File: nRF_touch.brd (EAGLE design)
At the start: 46 x 77.5 mm, 35 parts, among them J1 CORTEX_DEBUG_PTH, T1 BSS84, T2 BC847, U1 ADP160, U2 AT42QT1010-TSHR

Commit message: First routing
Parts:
- added C9: 0.1uF, SparkFun-Capacitors:0603
- added LED1: (no value), adafruit:CHIPLED_1206
- added R12: 330, SparkFun-Resistors:0603
- moved J1 36.3 mm to (44.2, 31.0), turned to 90 degrees
- moved J2 13.5 mm to (44.3, 13.2), turned to 90 degrees
- moved R3 1.31 mm to (40.6, 51.9), turned to 180 degrees
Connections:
- new net N$1: R12.2, U$1.D6
- new net N$2: LED1.A, R12.1
- net GND: now also C9.2, LED1.C
- net LDO_EN: now also C9.1
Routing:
- net VCC: track 0.00 -> 157.2 mm, vias 0 -> 8
- net 5V: track 0.00 -> 75.1 mm, vias 0 -> 4
- net GND: track 0.00 -> 61.6 mm, vias 0 -> 1
- net SPIM_DO: track 0.00 -> 49.7 mm, vias 0 -> 2
- net SPIM_SCK: track 0.00 -> 45.2 mm, vias 0 -> 2
- net AT42_OUT: track 0.00 -> 41.6 mm, vias 0 -> 2
- net SCL: track 0.00 -> 37.5 mm, vias 0 -> 1
- net SDA: track 0.00 -> 36.2 mm, vias 0 -> 1
- net SST_CS: track 0.00 -> 36.0 mm, vias 0 -> 2
- net SPIS_SCK: track 0.00 -> 31.5 mm, vias 0 -> 2
- net SPIM_DIN: track 0.00 -> 29.5 mm, vias 0 -> 2
- net SHARP_CS: track 0.00 -> 27.8 mm, vias 0 -> 2
- net 5150_CS: track 0.00 -> 27.0 mm, vias 0 -> 2
- net NRF_EN: track 0.00 -> 21.2 mm, vias 0 -> 2
- net SPIS_MI: track 0.00 -> 20.3 mm, vias 0 -> 2
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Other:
- board size 46 x 77.5 mm -> 46.3 x 77.5 mm

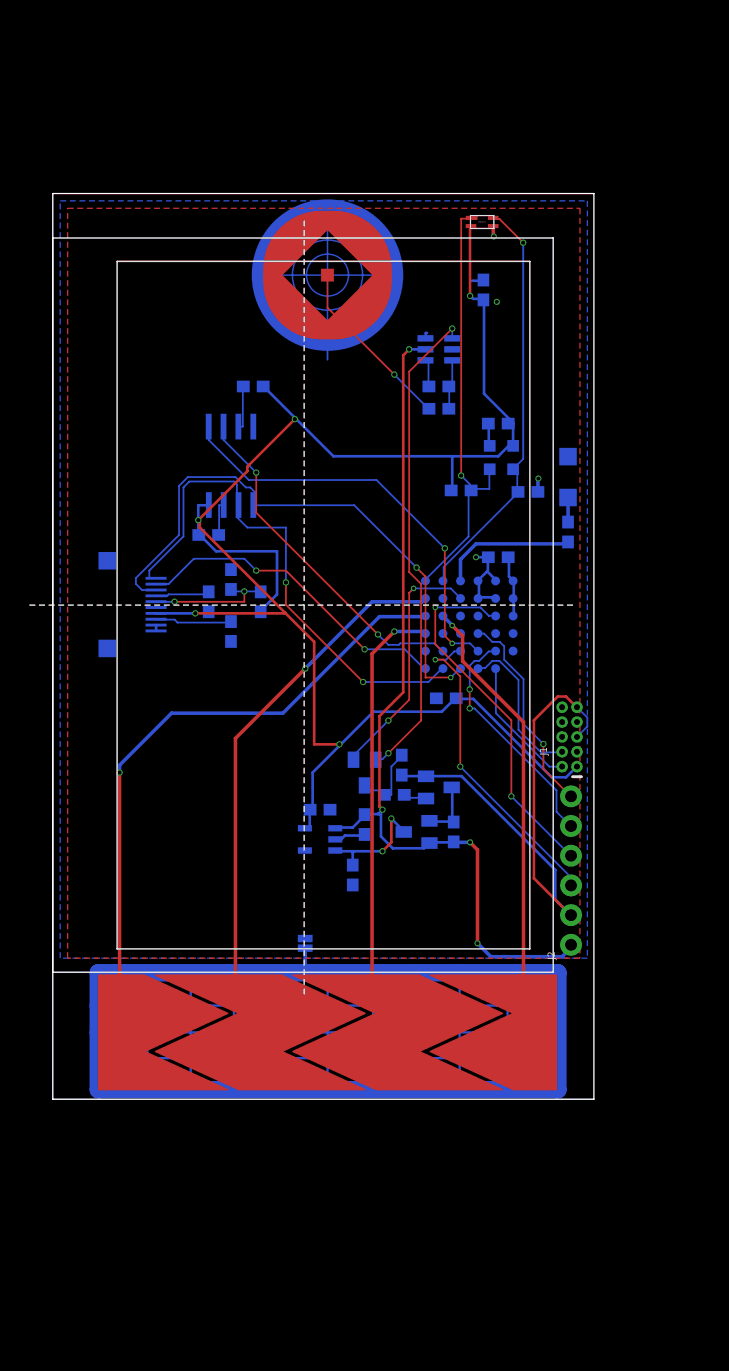
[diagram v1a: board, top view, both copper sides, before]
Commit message: Modified stop on qtouch
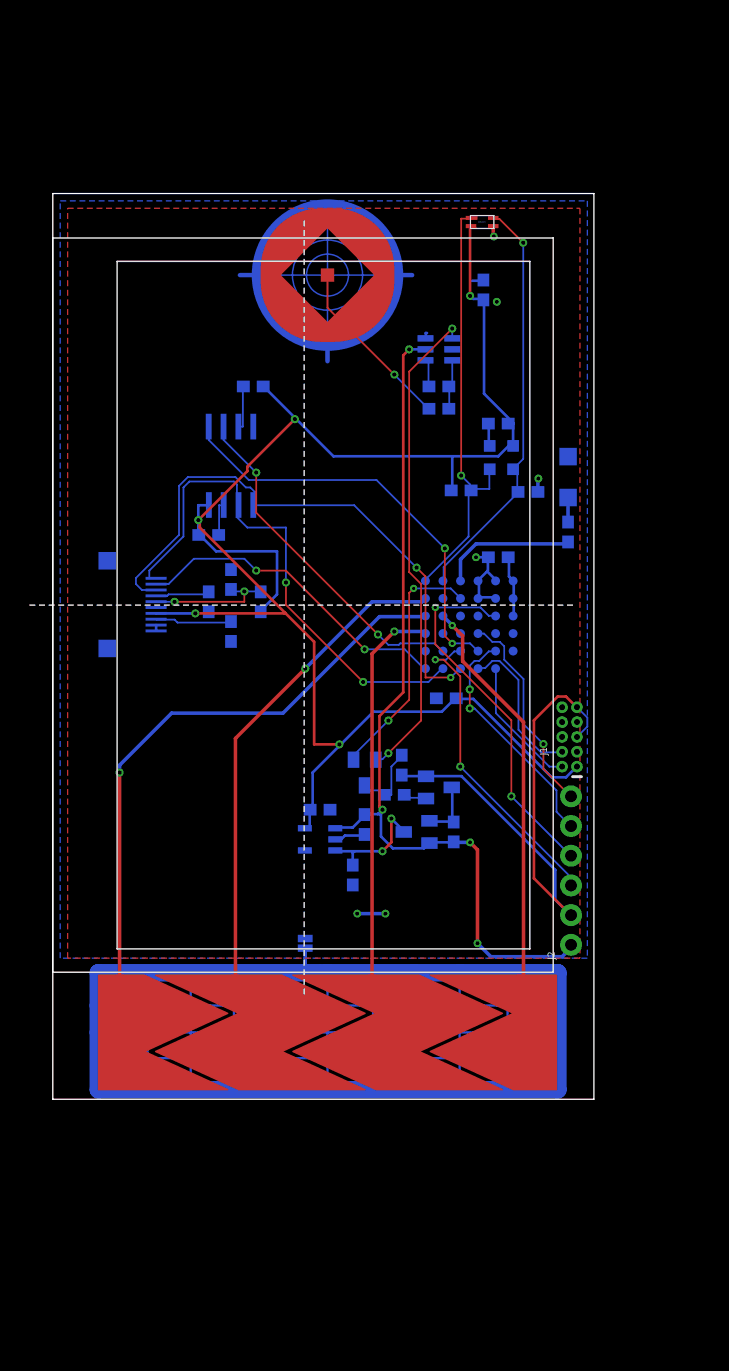
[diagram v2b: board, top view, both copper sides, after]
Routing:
- net GND: track 61.6 -> 65.5 mm
- net VCC: track 157.2 -> 159.6 mm, vias 8 -> 10
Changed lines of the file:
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@@
 <layers>
 <layer number="1" name="Top" color="4" fill="1" visible="yes" active="yes"/>
-<layer number="2" name="Route2" color="1" fill="3" visible="no" active="yes"/>
+<layer number="2" name="Route2" color="1" fill="3" visible="no" active="no"/>
 <layer number="3" name="Route3" color="4" fill="3" visible="no" active="no"/>
 <layer number="4" name="Route4" color="1" fill="4" visible="no" active="no"/>
@@
 <layer number="13" name="Route13" color="4" fill="5" visible="no" active="no"/>
 <layer number="14" name="Route14" color="1" fill="6" visible="no" active="no"/>
-<layer number="15" name="Route15" color="4" fill="6" visible="no" active="yes"/>
+<layer number="15" name="Route15" color="4" fill="6" visible="no" active="no"/>
 <layer number="16" name="Bottom" color="1" fill="1" visible="yes" active="yes"/>
 <layer number="17" name="Pads" color="2" fill="1" visible="yes" active="yes"/>
@@
 <layer number="41" name="tRestrict" color="4" fill="10" visible="yes" active="yes"/>
 <layer number="42" name="bRestrict" color="1" fill="10" visible="yes" active="yes"/>
-<layer number="43" name="vRestrict" color="2" fill="10" visible="yes" active="yes"/>
+<layer number="43" name="vRestrict" color="2" fill="10" visible="no" active="yes"/>
 <layer number="44" name="Drills" color="7" fill="1" visible="no" active="yes"/>
 <layer number="45" name="Holes" color="7" fill="1" visible="no" active="yes"/>
@@
 </class>
 </classes>
-<designrules name="OSHPark-4layer">
+<designrules name="oshpark-2layer">
 <description language="de">&lt;b&gt;EAGLE Design Rules&lt;/b&gt;
 &lt;p&gt;
@@
 &lt;p&gt;
 Please make sure your boards conform to these design rules.</description>
-<param name="layerSetup" value="(1*2*15*16)"/>
-<param name="mtCopper" value="0.035559375mm 0.01778125mm 0.0356mm 0.0356mm 0.0356mm 0.0356mm 0.0356mm 0.0356mm 0.0356mm 0.0356mm 0.0356mm 0.0356mm 0.0356mm 0.0356mm 0.01778125mm 0.035559375mm"/>
-<param name="mtIsolate" value="0.17018125mm 47mil 0.2007mm 0.1499mm 0.2007mm 0.1499mm 0.2007mm 0.1499mm 0.2007mm 0.1499mm 0.2007mm 0.1499mm 0.2007mm 0.1499mm 0.17018125mm"/>
-<param name="mdWireWire" value="5mil"/>
-<param name="mdWirePad" value="5mil"/>
-<param name="mdWireVia" value="5mil"/>
-<param name="mdPadPad" value="5mil"/>
-<param name="mdPadVia" value="5mil"/>
-<param name="mdViaVia" value="5mil"/>
-<param name="mdSmdPad" value="5mil"/>
-<param name="mdSmdVia" value="5mil"/>
-<param name="mdSmdSmd" value="5mil"/>
+<param name="layerSetup" value="(1*16)"/>
+<param name="mtCopper" value="0.0356mm 0.0356mm 0.0356mm 0.0356mm 0.0356mm 0.0356mm 0.0356mm 0.0356mm 0.0356mm 0.0356mm 0.0356mm 0.0356mm 0.0356mm 0.0356mm 0.0356mm 0.0356mm"/>
+<param name="mtIsolate" value="1.5011mm 0.1499mm 0.2007mm 0.1499mm 0.2007mm 0.1499mm 0.2007mm 0.1499mm 0.2007mm 0.1499mm 0.2007mm 0.1499mm 0.2007mm 0.1499mm 0.2007mm"/>
+<param name="mdWireWire" value="6mil"/>
+<param name="mdWirePad" value="6mil"/>
+<param name="mdWireVia" value="6mil"/>
+<param name="mdPadPad" value="6mil"/>
+<param name="mdPadVia" value="6mil"/>
+<param name="mdViaVia" value="6mil"/>
+<param name="mdSmdPad" value="6mil"/>
+<param name="mdSmdVia" value="6mil"/>
+<param name="mdSmdSmd" value="6mil"/>
 <param name="mdViaViaSameLayer" value="8mil"/>
 <param name="mnLayersViaInSmd" value="2"/>
@@
 <param name="mdDrill" value="6mil"/>
 <param name="mdSmdStop" value="0mil"/>
-<param name="msWidth" value="5mil"/>
-<param name="msDrill" value="10mil"/>
-<param name="msMicroVia" value="10mil"/>
+<param name="msWidth" value="6mil"/>
+<param name="msDrill" value="13mil"/>
+<param name="msMicroVia" value="13mil"/>
 <param name="msBlindViaRatio" value="0.5"/>
 <param name="rvPadTop" value="0.25"/>
@@
 <param name="rvMicroViaOuter" value="0.25"/>
 <param name="rvMicroViaInner" value="0.25"/>
-<param name="rlMinPadTop" value="4mil"/>
+<param name="rlMinPadTop" value="7mil"/>
 <param name="rlMaxPadTop" value="20mil"/>
-<param name="rlMinPadInner" value="4mil"/>
+<param name="rlMinPadInner" value="7mil"/>
 <param name="rlMaxPadInner" value="20mil"/>
-<param name="rlMinPadBottom" value="4mil"/>
+<param name="rlMinPadBottom" value="7mil"/>
 <param name="rlMaxPadBottom" value="20mil"/>
-<param name="rlMinViaOuter" value="4mil"/>
+<param name="rlMinViaOuter" value="7mil"/>
 <param name="rlMaxViaOuter" value="20mil"/>
-<param name="rlMinViaInner" value="4mil"/>
+<param name="rlMinViaInner" value="7mil"/>
 <param name="rlMaxViaInner" value="20mil"/>
 <param name="rlMinMicroViaOuter" value="4mil"/>
@@
 <via x="36.195" y="46.355" extent="1-16" drill="0.3302"/>
 <wire x1="36.195" y1="46.355" x2="37.25" y2="46.355" width="0.2286" layer="16"/>
+<via x="26.035" y="15.875" extent="1-16" drill="0.3302"/>
+<via x="28.448" y="15.875" extent="1-16" drill="0.3302"/>
+<wire x1="26.035" y1="15.875" x2="28.448" y2="15.875" width="0.3048" layer="16"/>
 </signal>
 <signal name="GND" class="1">
@@
 <wire x1="37.669" y1="73.837" x2="37.719" y2="73.787" width="0.3048" layer="1"/>
 <wire x1="23.495" y1="64.516" x2="23.495" y2="64.397" width="0.1524" layer="16"/>
-<wire x1="23.495" y1="64.397" x2="23.495" y2="63.246" width="0.1524" layer="16"/>
+<wire x1="23.495" y1="64.397" x2="23.495" y2="64.389" width="0.1524" layer="16"/>
+<wire x1="23.495" y1="64.389" x2="23.495" y2="63.246" width="0.1524" layer="16"/>
 <wire x1="44.831" y1="33.528" x2="45.72" y2="32.639" width="0.1524" layer="16"/>
 <wire x1="45.72" y1="32.639" x2="45.72" y2="31.877" width="0.1524" layer="16"/>
 <wire x1="45.72" y1="31.877" x2="44.831" y2="30.988" width="0.1524" layer="16"/>
+<wire x1="23.495" y1="63.119" x2="23.495" y2="64.389" width="0.381" layer="16"/>
+<wire x1="16.002" y1="70.485" x2="17.399" y2="70.485" width="0.381" layer="16"/>
+<wire x1="29.464" y1="70.485" x2="30.734" y2="70.485" width="0.381" layer="16"/>
 </signal>
 <signal name="AIN2">

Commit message: Improvements #1
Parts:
- added C10: 0.1uF, SparkFun-Capacitors:0603
- U$4: value SHARP27_REV -> SHARP27
- moved R5 9.19 mm to (10.1, 47.6), turned to 45 degrees
- moved LED1 4.32 mm to (44.1, 57.5)
- moved R12 3.56 mm to (44.1, 52.1)
- moved U$4 0.44 mm to (6.16, 42.2)
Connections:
- net 5V: now also C10.2
- net DISP: now also U$4.5; no longer U$4.6
- net EXTCOMM: now also U$4.4; no longer U$4.7
- net EXTMODE: now also U$4.8; no longer U$4.3
- net GND: now also C10.1, U$4.10, U$4.9; no longer U$4.1, U$4.2
- net SHARP_CS: now also U$4.3; no longer U$4.9
- net SPIM_DO: now also U$4.2; no longer U$4.8
- net SPIM_SCK: now also U$4.1; no longer U$4.10
- net VCC: now also U$4.6, U$4.7; no longer U$4.4
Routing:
- net VCC: track 159.6 -> 50.1 mm, vias 10 -> 13
- net SPIM_SCK: track 45.2 -> 39.4 mm, vias 2 -> 3
- net GND: track 65.5 -> 69.8 mm, vias 1 -> 3
- net 5V: track 75.1 -> 78.6 mm
- net SPIM_DO: track 49.7 -> 52.3 mm
- net EXTMODE: track 6.61 -> 5.08 mm
- net N$1: track 11.7 -> 13.1 mm
- net N$2: track 2.10 -> 2.86 mm
- net DISP: track 11.1 -> 10.4 mm, vias 2 -> 0

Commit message: Optimizations
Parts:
- moved JP1 1.98 mm to (22.9, 11.8)
- moved C5 0.38 mm to (33.3, 34.3)
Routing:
- net N$10: track 2.76 -> 0.03 mm
- net LDO_EN: track 10.1 -> 8.40 mm
- net SPIM_SCK: track 39.4 -> 41.0 mm
- net SCL: track 37.5 -> 36.5 mm
- net VCC: track 50.1 -> 50.6 mm

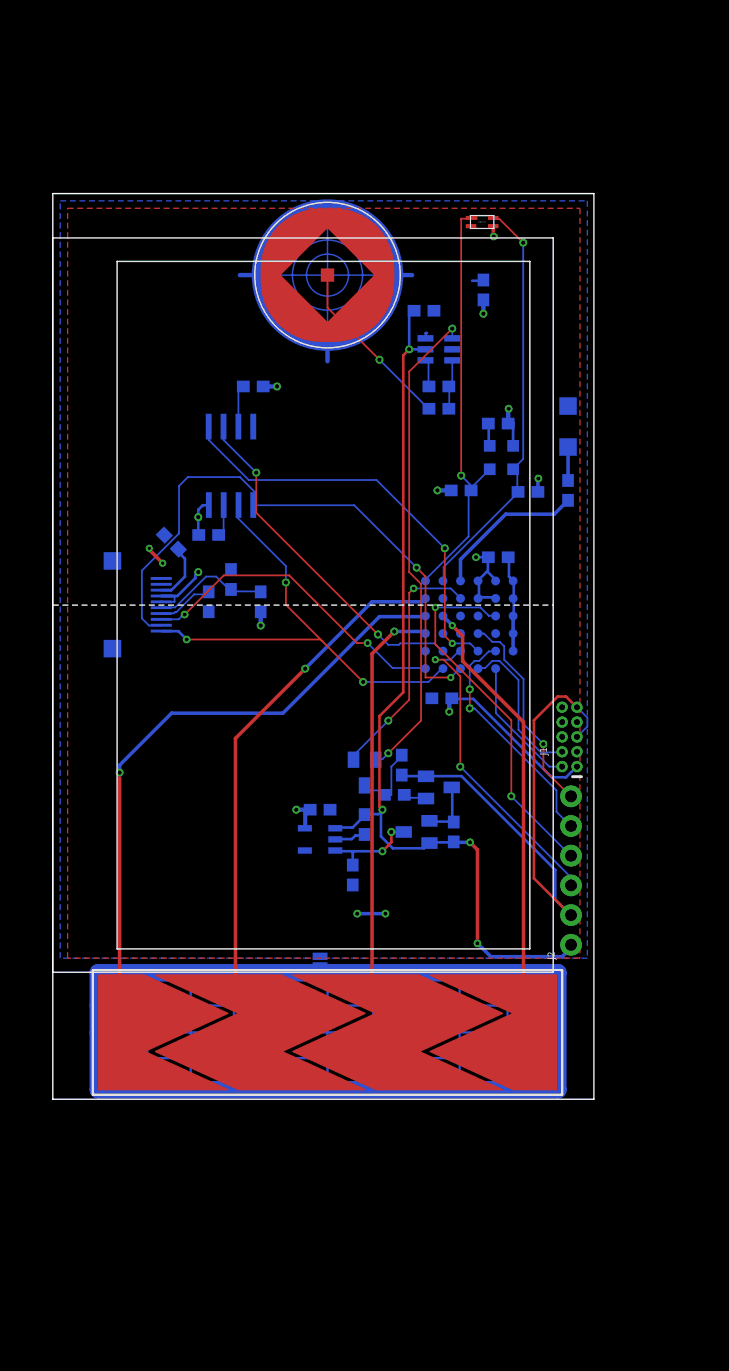
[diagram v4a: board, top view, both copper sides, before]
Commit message: Addition of neopixel and change in logic
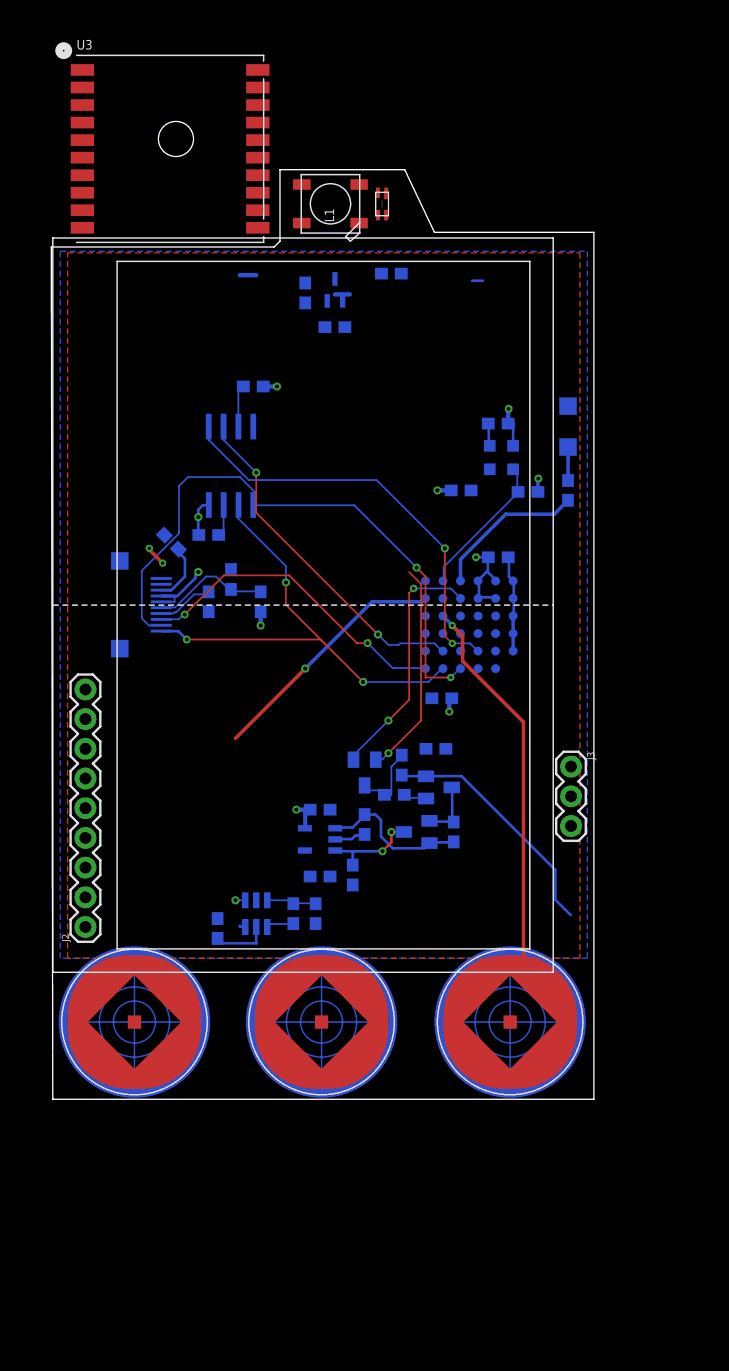
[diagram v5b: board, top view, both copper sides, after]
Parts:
- removed J1: CORTEX_DEBUG_PTH, SparkFun-Connectors:2X5-PTH-1.27MM
- removed JP1: (no value), SparkFun-Retired:SJ_2S
- added C11: 1uF, SparkFun-Capacitors:0603
- added J3: (no value), SparkFun-Connectors:1X03
- added L1: WS2812B, adafruit:WS2812B
- added Q1: BSS138BKW, BSS138:SOT65P210X110-3N
- added R13: 47k, SparkFun-Resistors:0603
- added R14, R15: 10k, SparkFun-Resistors:0603
- added S3: L_BUTTON, qtouch:BUTTON
- added U3: (no value), adafruit:FGPMMOPA6H
- D1: value BAT754C -> BAT54C
- J2: device SparkFun-Connectors:1X06_NO_SILK -> SparkFun-Connectors:1X09
- S1: value SLIDER -> L_BUTTON; device qtouch:SLIDER -> qtouch:BUTTON
- T2: value BC847 -> BC847/2N7002
- moved S2 63.9 mm to (23.0, 6.60)
- moved C10 55.7 mm to (14.1, 14.6), turned to 270 degrees
- moved U2 50.7 mm to (17.4, 15.9), turned to 270 degrees
- moved C7 46.8 mm to (20.6, 15.9), turned to 90 degrees
- moved R11 44.4 mm to (22.5, 15.9), turned to 90 degrees
- moved J2 41.6 mm to (2.79, 14.7)
- moved S1 15.6 mm to (39.1, 6.60)
- moved U$2 9.95 mm to (27.8, 75.6), turned to 90 degrees
- moved C3 8.00 mm to (29.0, 70.6), turned to 0 degrees
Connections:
- removed net AIN2: S1.P$1, U$1.F4
- removed net AIN4: S1.P$3, U$1.F3
- removed net LDO_EN: C9.1, T1.3, U1.3
- removed net N$10: JP1.1, S1.GND
- new net NEO_DIN: L1.4-DIN, Q1.3, R14.1
- new net NEO_PIN: Q1.2, R15.1, U$1.F1
- new net SW_POWER: C9.1, L1.1-VDD, R13.2, R14.2, T1.3, U1.3
- net AIN3: now also S3.P$1; no longer S1.P$2
- net AIN5: now also S1.P$1; no longer S1.P$4
- net GND: now also C11.2, L1.3-GND, R13.1, S1.GND, S3.GND; no longer J1.3, J1.5, J1.9, JP1.2
- net N$11: now also C11.1
- net SHARP_CS: no longer U$1.F1
- net SPIS_MI: no longer U$1.B2
- net SPIS_MO: no longer U$1.C3
- net SPIS_SCK: no longer U$1.B4
- net SST_CS: now also J2.7; no longer U$1.C2
- net SWDCLK: now also J3.2; no longer J1.4
- net SWDIO: now also J3.1; no longer J1.2
- net VCC: now also J2.9, J3.3, Q1.1, R15.2; no longer J1.1
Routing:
- net 5V: track 78.5 -> 17.9 mm, vias 4 -> 0
- net AIN2: track 50.0 -> 0.00 mm, vias 1 -> 0
- net SCL: track 36.5 -> 0.00 mm, vias 1 -> 0
- net AIN4: track 33.5 -> 0.00 mm, vias 1 -> 0
- net SPIS_SCK: track 31.5 -> 0.00 mm, vias 2 -> 0
- net GND: track 69.8 -> 40.0 mm, vias 3 -> 2
- net 5150_CS: track 27.0 -> 0.00 mm, vias 2 -> 0
- net SDA: track 36.2 -> 13.0 mm, vias 1 -> 0
- net AT42_OUT: track 41.6 -> 19.2 mm
- net AIN3: track 42.0 -> 21.2 mm
- net SPIS_MI: track 20.3 -> 0.00 mm, vias 2 -> 0
- net SPIS_MO: track 17.9 -> 0.00 mm, vias 1 -> 0
- net VCC: track 50.6 -> 32.8 mm, vias 13 -> 10
- net PAD: track 15.0 -> 0.04 mm, vias 1 -> 0
- net SWDCLK: track 13.2 -> 0.00 mm
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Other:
- board size 46.3 x 77.5 mm -> 46.4 x 79.5 mm
